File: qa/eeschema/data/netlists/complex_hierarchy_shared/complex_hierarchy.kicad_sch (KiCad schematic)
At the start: 10 parts, among them P1 CONN_2, P2 CONN_2, U1 78L05, U2 ICL7660

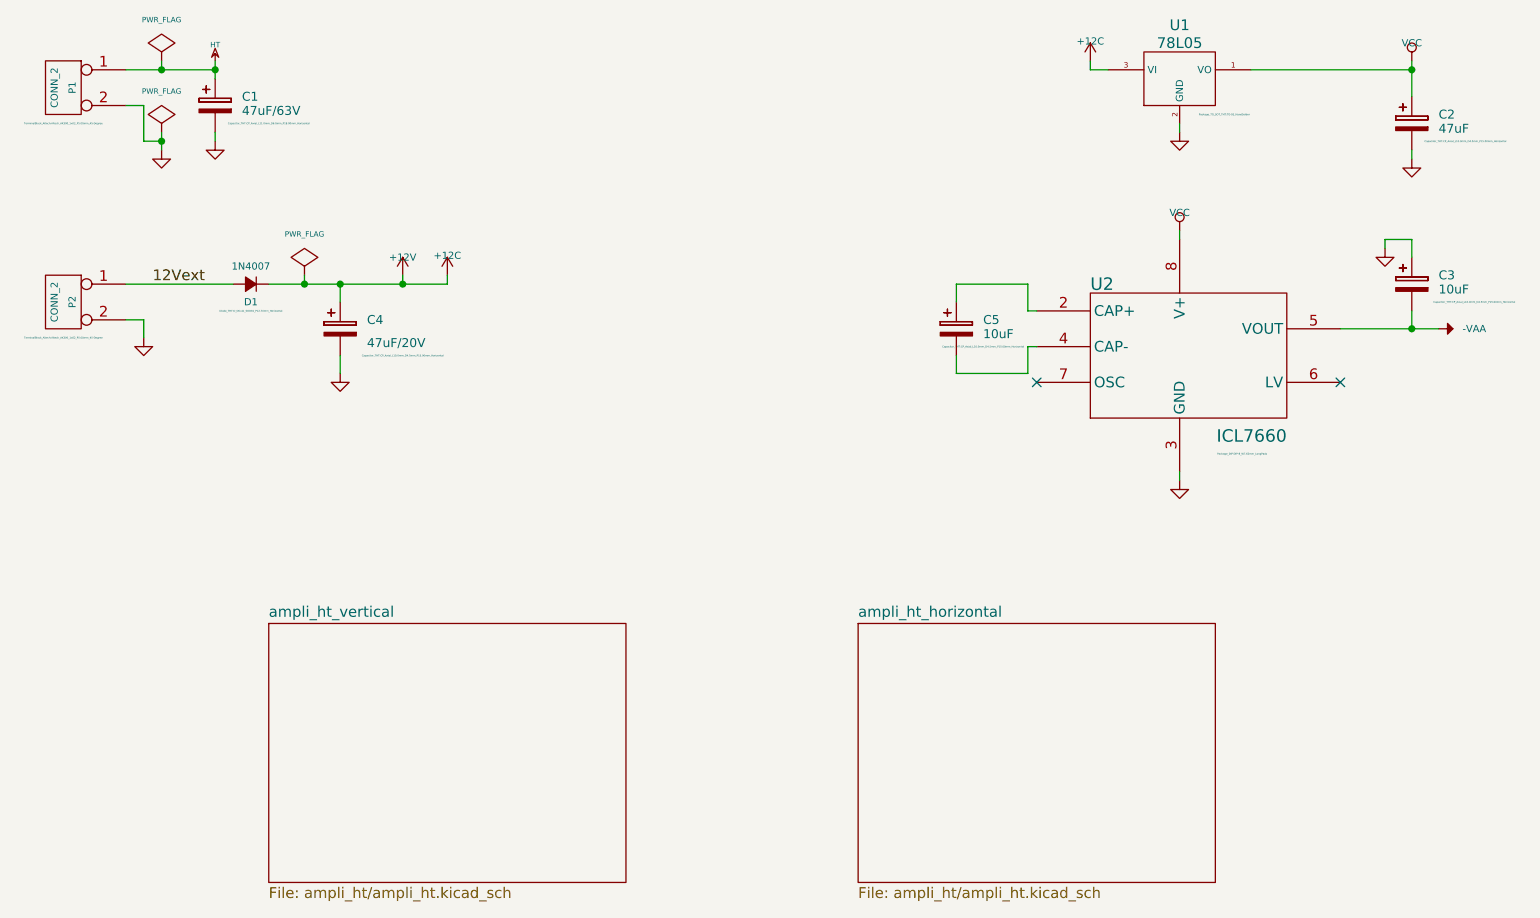
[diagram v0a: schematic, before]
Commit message: Fix duplicate UUIDs in test cases.
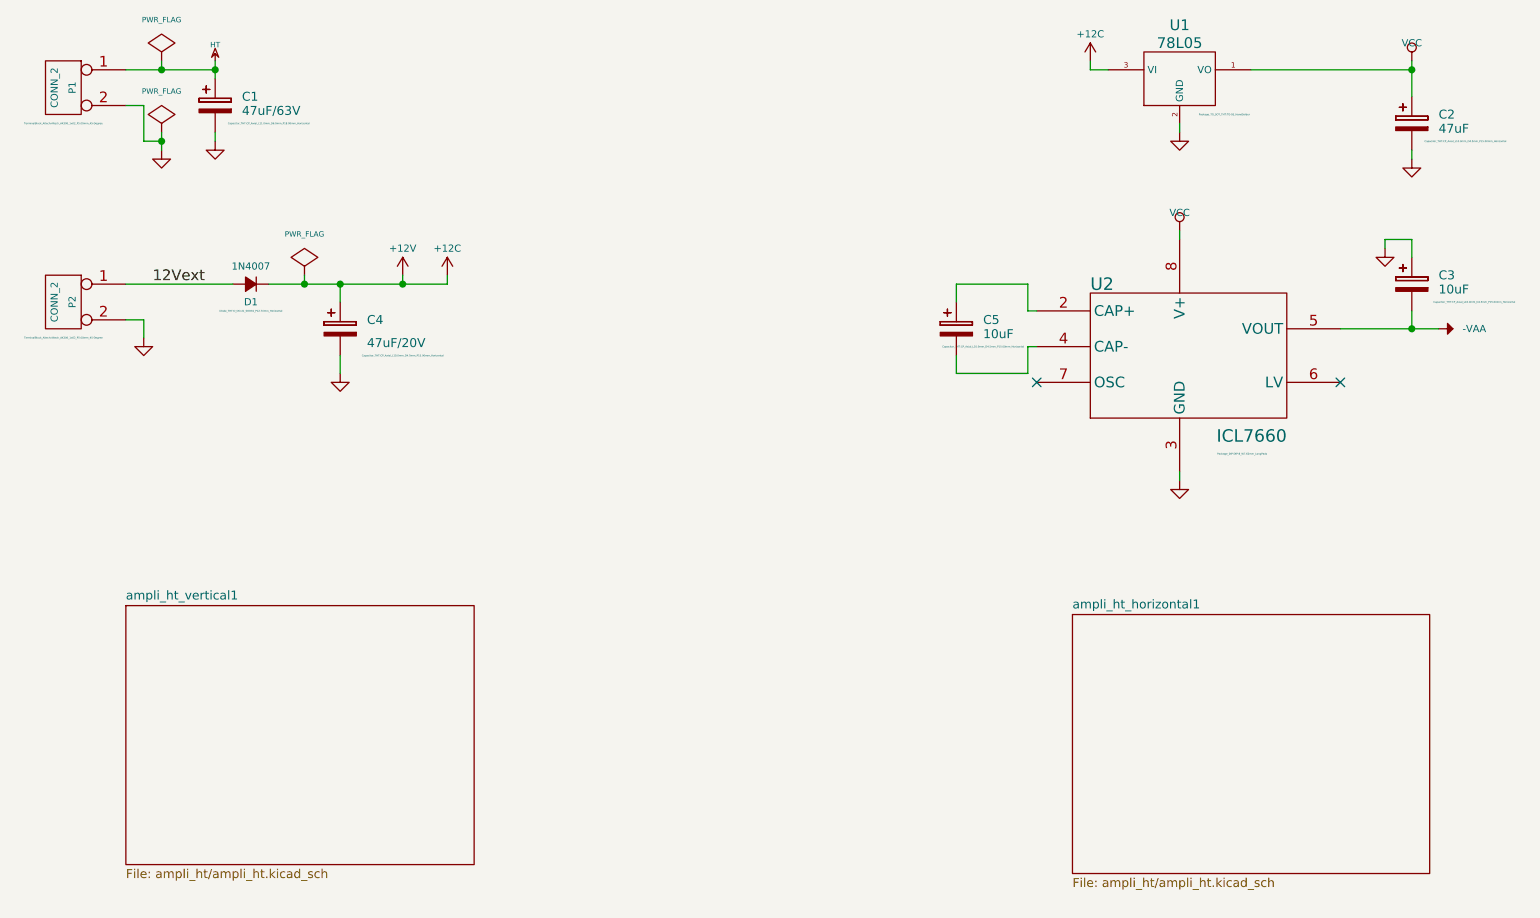
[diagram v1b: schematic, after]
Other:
- removed sheet ampli_ht_horizontal
- removed sheet ampli_ht_vertical
- added sheet ampli_ht_horizontal1 (ampli_ht/ampli_ht.kicad_sch)
- added sheet ampli_ht_vertical1 (ampli_ht/ampli_ht.kicad_sch)
